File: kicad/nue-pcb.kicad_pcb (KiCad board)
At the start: 2 copper layers, 293.9 x 103.4 mm, 160 parts, among them J1 Conn_01x04, J2 AVR-ISP-6, SW1 ESC, SW10 9, SW11 0, SW12 -, SW13 =, SW14 2U BACKSP, SW15 TAB150, SW16 Q, SW17 W, SW18 E, SW19 R, SW2 1, SW20 T, SW21 Y, SW22 U, SW23 I, SW24 O, SW25 P, SW26 CURL_L, SW27 CURL_R, SW28 1U RBKSP, SW29 CAPS, SW3 2, SW30 A, SW31 S, SW32 D, SW33 F, SW34 G, SW35 H, SW36 J, SW37 K, SW38 L, SW39 ;, SW4 3, SW40 ', SW41 PIPE150, SW42 ENTER_ANSI, SW43 LSHIFT225, SW44 ISO_PIPE, SW45 Z, SW46 X, SW47 C, SW48 V, SW49 B, SW5 4, SW50 N, SW51 M, SW52 <, SW53 >, SW54 ?, SW55 RSHIFT275, SW56 FN, SW57 LCTRL125, SW58 LWIN125, SW59 LALT125, SW6 5, SW60 SPACE625, SW61 RALT125, SW62 RWIN125, SW63 MENU, SW64 RCTRL125, SW65 1U LBACKSP, SW66 STEPPEDCAPS, SW67 ENTER_ISO, SW68 LSHIFT125, SW69 RSHIFT175, SW7 6, SW70 LCTRL150, SW71 LWIN100, SW72 LALT150, SW73 SPACE700, SW74 RALT150, SW75 RWIN100, SW76 RCTRL150, SW77 PIPE100, SW8 7, SW9 8, U1 ATmega32U4-MU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

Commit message: ouro modifications
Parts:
- H2: footprint kestralib:nue-logo -> bachoologos:bachoo_smol
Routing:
- net Col13: track 370.2 -> 367.3 mm
- net Col3: track 132.7 -> 130.2 mm
- net Col11: track 297.1 -> 294.7 mm
- net GND: track 125.9 -> 123.6 mm
- net Col10: track 273.1 -> 270.7 mm
- net Col12: track 321.6 -> 319.3 mm
- net Col6: track 166.9 -> 164.7 mm
- net Col5: track 148.9 -> 146.7 mm
- net Col4: track 130.2 -> 128.1 mm
- net VCC: track 140.3 -> 138.6 mm
- net Col7: track 215.6 -> 213.8 mm
- net Col2: track 109.6 -> 107.8 mm
- net Col8: track 202.8 -> 201.0 mm
- net Col9: track 222.5 -> 220.8 mm
- net RESET: track 75.7 -> 74.0 mm
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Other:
- board size 293.9 x 103.4 mm -> 286.7 x 105.2 mm
- board text added: "Nue PCB Revision 1.1-B"
- board text removed: "Nue PCB Revision 1.1"

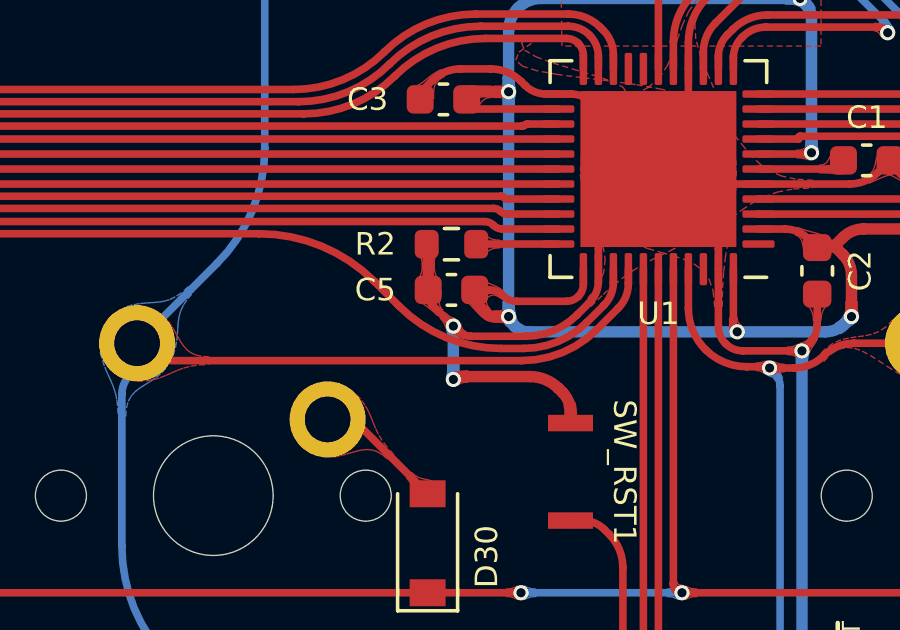
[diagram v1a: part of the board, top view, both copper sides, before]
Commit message: fixed spacing issue
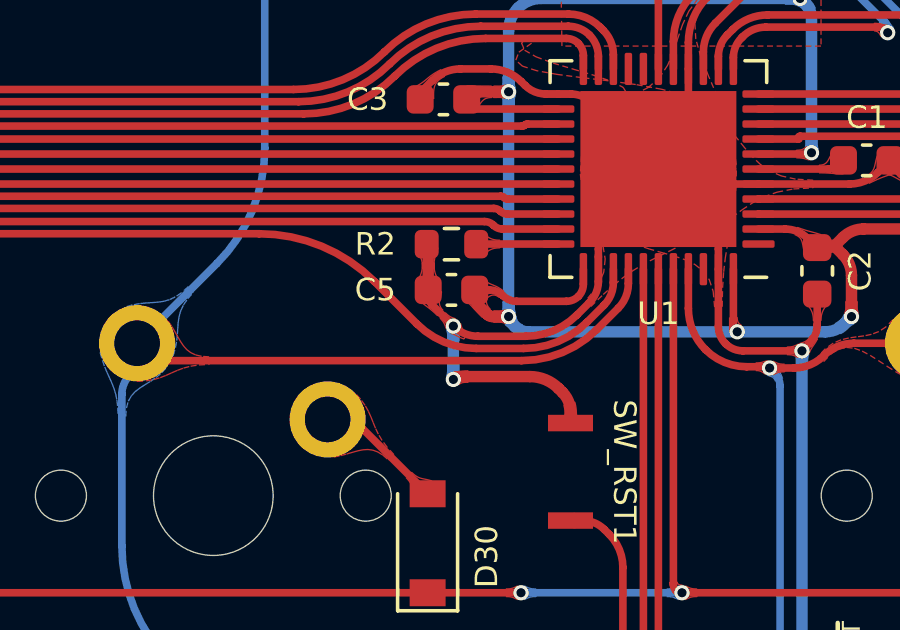
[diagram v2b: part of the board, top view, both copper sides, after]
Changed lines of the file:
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@@
   )
   (segment (start 316.102326 98.3615) (end 318.0715 98.3615) (width 0.254) (layer "F.Cu") (net 1))
-  (segment (start 306.62045 97.70545) (end 306.451 97.536) (width 0.254) (layer "F.Cu") (net 1))
   (segment (start 313.746999 80.460999) (end 313.661508 80.546491) (width 0.254) (layer "F.Cu") (net 1))
   (segment (start 310.36675 89.801) (end 309.948 89.801) (width 0.254) (layer "F.Cu") (net 1))
@@
   (segment (start 336.202797 76.360797) (end 334.786225 74.944225) (width 0.381) (layer "F.Cu") (net 1))
   (segment (start 316.623 92.801) (end 313.7855 92.801) (width 0.254) (layer "F.Cu") (net 1))
-  (segment (start 308.855175 97.874901) (end 307.02954 97.874901) (width 0.254) (layer "F.Cu") (net 1))
+  (segment (start 308.855175 97.874901) (end 307.269065 97.874901) (width 0.254) (layer "F.Cu") (net 1))
   (segment (start 306.6907 88.9635) (end 307.700298 88.9635) (width 0.254) (layer "F.Cu") (net 1))
   (segment (start 315.2855 95.6385) (end 315.2855 94.96975) (width 0.254) (layer "F.Cu") (net 1))
@@
   (arc (start 336.202797 76.360797) (mid 337.382376 78.126162) (end 337.79659 80.208553) (width 0.381) (layer "F.Cu") (net 1))
   (arc (start 313.4865 82.631789) (mid 313.473505 82.697117) (end 313.4365 82.7525) (width 0.254) (layer "F.Cu") (net 1))
-  (arc (start 306.62045 97.70545) (mid 306.808142 97.830862) (end 307.02954 97.874901) (width 0.254) (layer "F.Cu") (net 1))
+  (arc (start 306.451 97.536) (mid 306.826376 97.786845) (end 307.269065 97.874901) (width 0.254) (layer "F.Cu") (net 1))
   (arc (start 311.0816 90.0971) (mid 310.753624 89.877953) (end 310.36675 89.801) (width 0.254) (layer "F.Cu") (net 1))
   (arc (start 317.101723 81.008723) (mid 316.206494 80.41055) (end 315.1505 80.2005) (width 0.254) (layer "F.Cu") (net 1))
@@
   (segment (start 282.763963 94.4575) (end 299.975536 94.4575) (width 0.254) (layer "F.Cu") (net 11))
   (segment (start 278.916207 96.051292) (end 276.86 98.1075) (width 0.254) (layer "F.Cu") (net 11))
-  (segment (start 308.04175 98.281311) (end 308.788996 98.281311) (width 0.254) (layer "F.Cu") (net 11))
-  (segment (start 304.647272 96.875272) (end 303.823292 96.051292) (width 0.254) (layer "F.Cu") (net 11))
+  (segment (start 307.21466 98.281311) (end 308.788996 98.281311) (width 0.254) (layer "F.Cu") (net 11))
+  (segment (start 305.232113 97.460113) (end 303.823292 96.051292) (width 0.254) (layer "F.Cu") (net 11))
   (segment (start 310.907844 97.403655) (end 311.471721 96.839778) (width 0.254) (layer "F.Cu") (net 11))
   (arc (start 310.907844 97.403655) (mid 309.935708 98.053215) (end 308.788996 98.281311) (width 0.254) (layer "F.Cu") (net 11))
   (arc (start 282.763963 94.4575) (mid 280.681572 94.871713) (end 278.916207 96.051292) (width 0.254) (layer "F.Cu") (net 11))
   (arc (start 303.823292 96.051292) (mid 302.057926 94.871713) (end 299.975536 94.4575) (width 0.254) (layer "F.Cu") (net 11))
-  (arc (start 304.647272 96.875272) (mid 306.204671 97.915893) (end 308.04175 98.281311) (width 0.254) (layer "F.Cu") (net 11))
+  (arc (start 305.232113 97.460113) (mid 306.141713 98.067888) (end 307.21466 98.281311) (width 0.254) (layer "F.Cu") (net 11))
   (arc (start 311.7855 96.08225) (mid 311.703951 96.492221) (end 311.471721 96.839778) (width 0.254) (layer "F.Cu") (net 11))
   (segment (start 281.6225 69.754463) (end 281.6225 78.74) (width 0.254) (layer "B.Cu") (net 11))
